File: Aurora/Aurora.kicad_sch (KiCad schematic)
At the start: 28 parts, among them J1 UJ20-C-H-C-3-SMT-TR, U1 STM32H757BITx

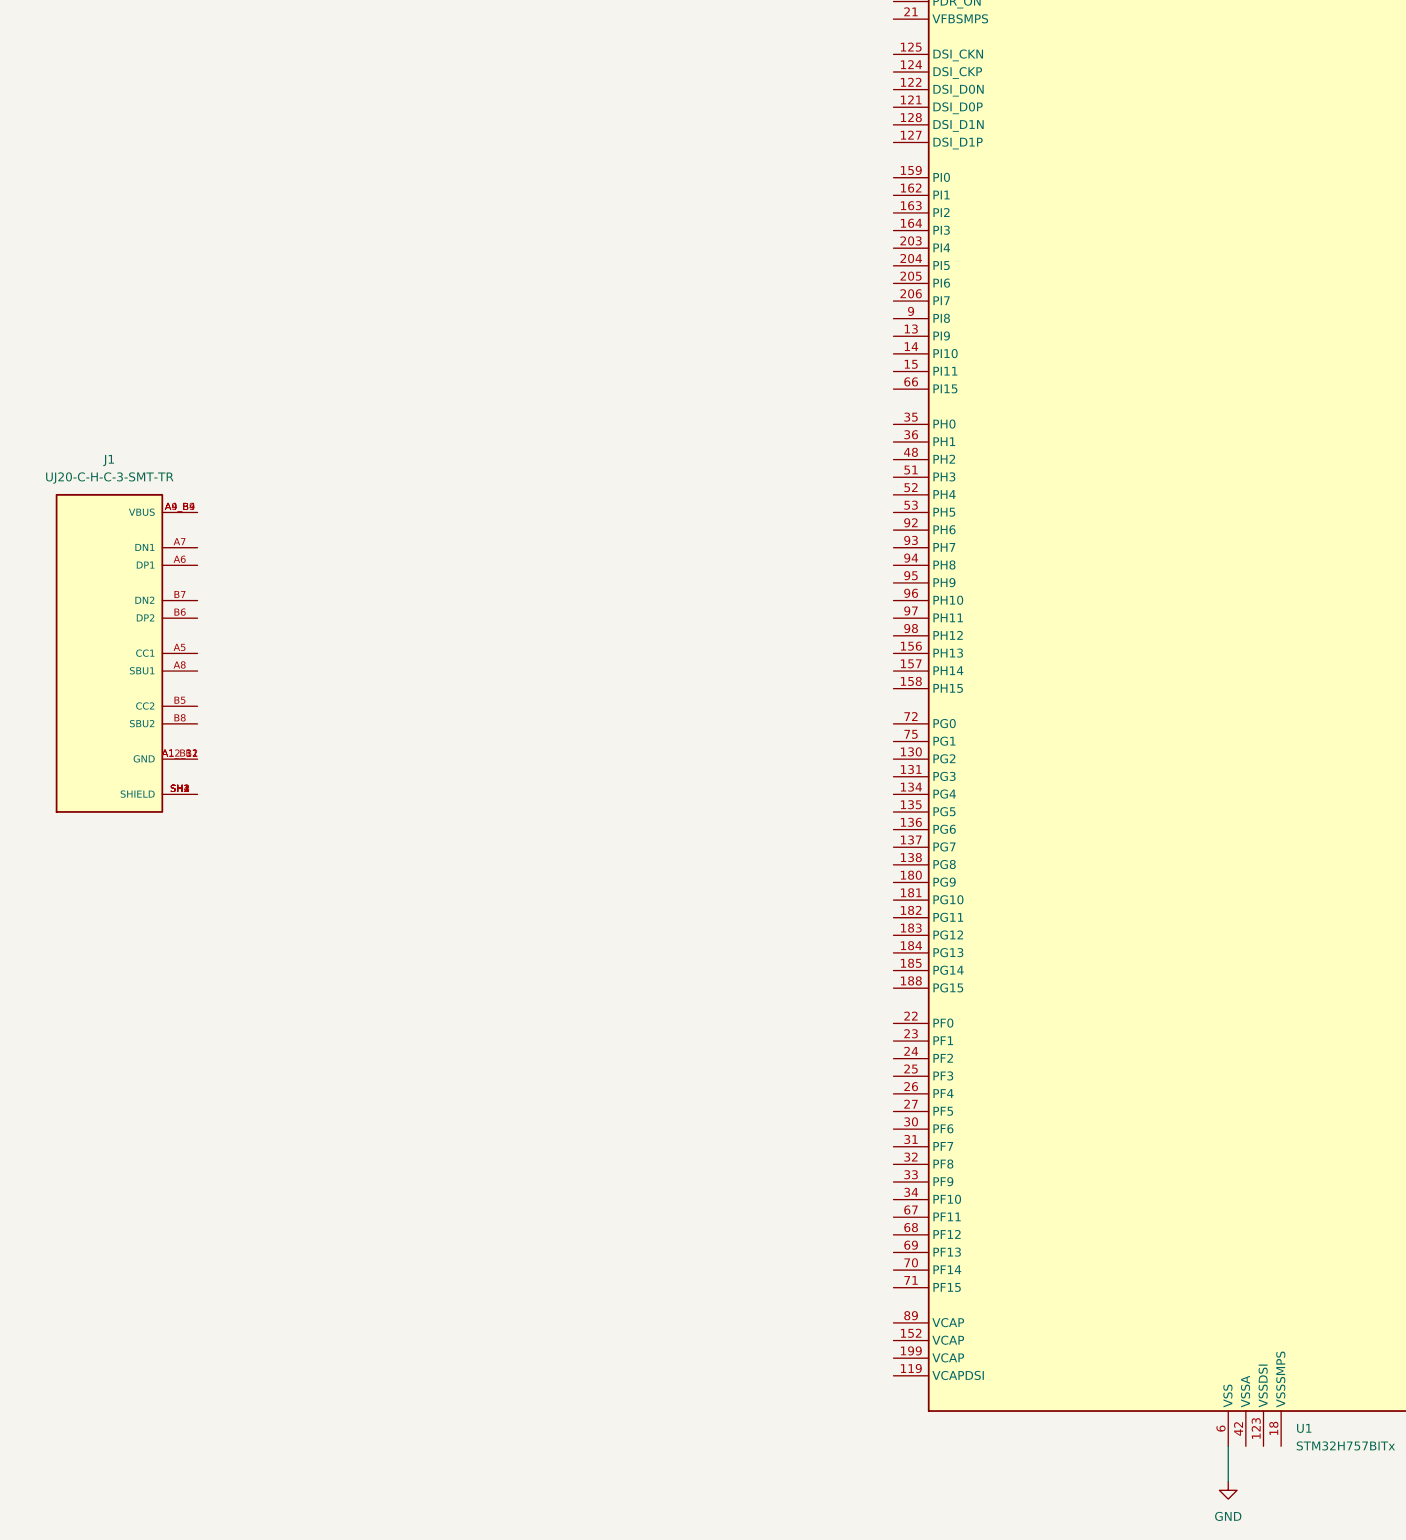
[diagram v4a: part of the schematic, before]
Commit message: hooked up USB receptacle, added ESD protection
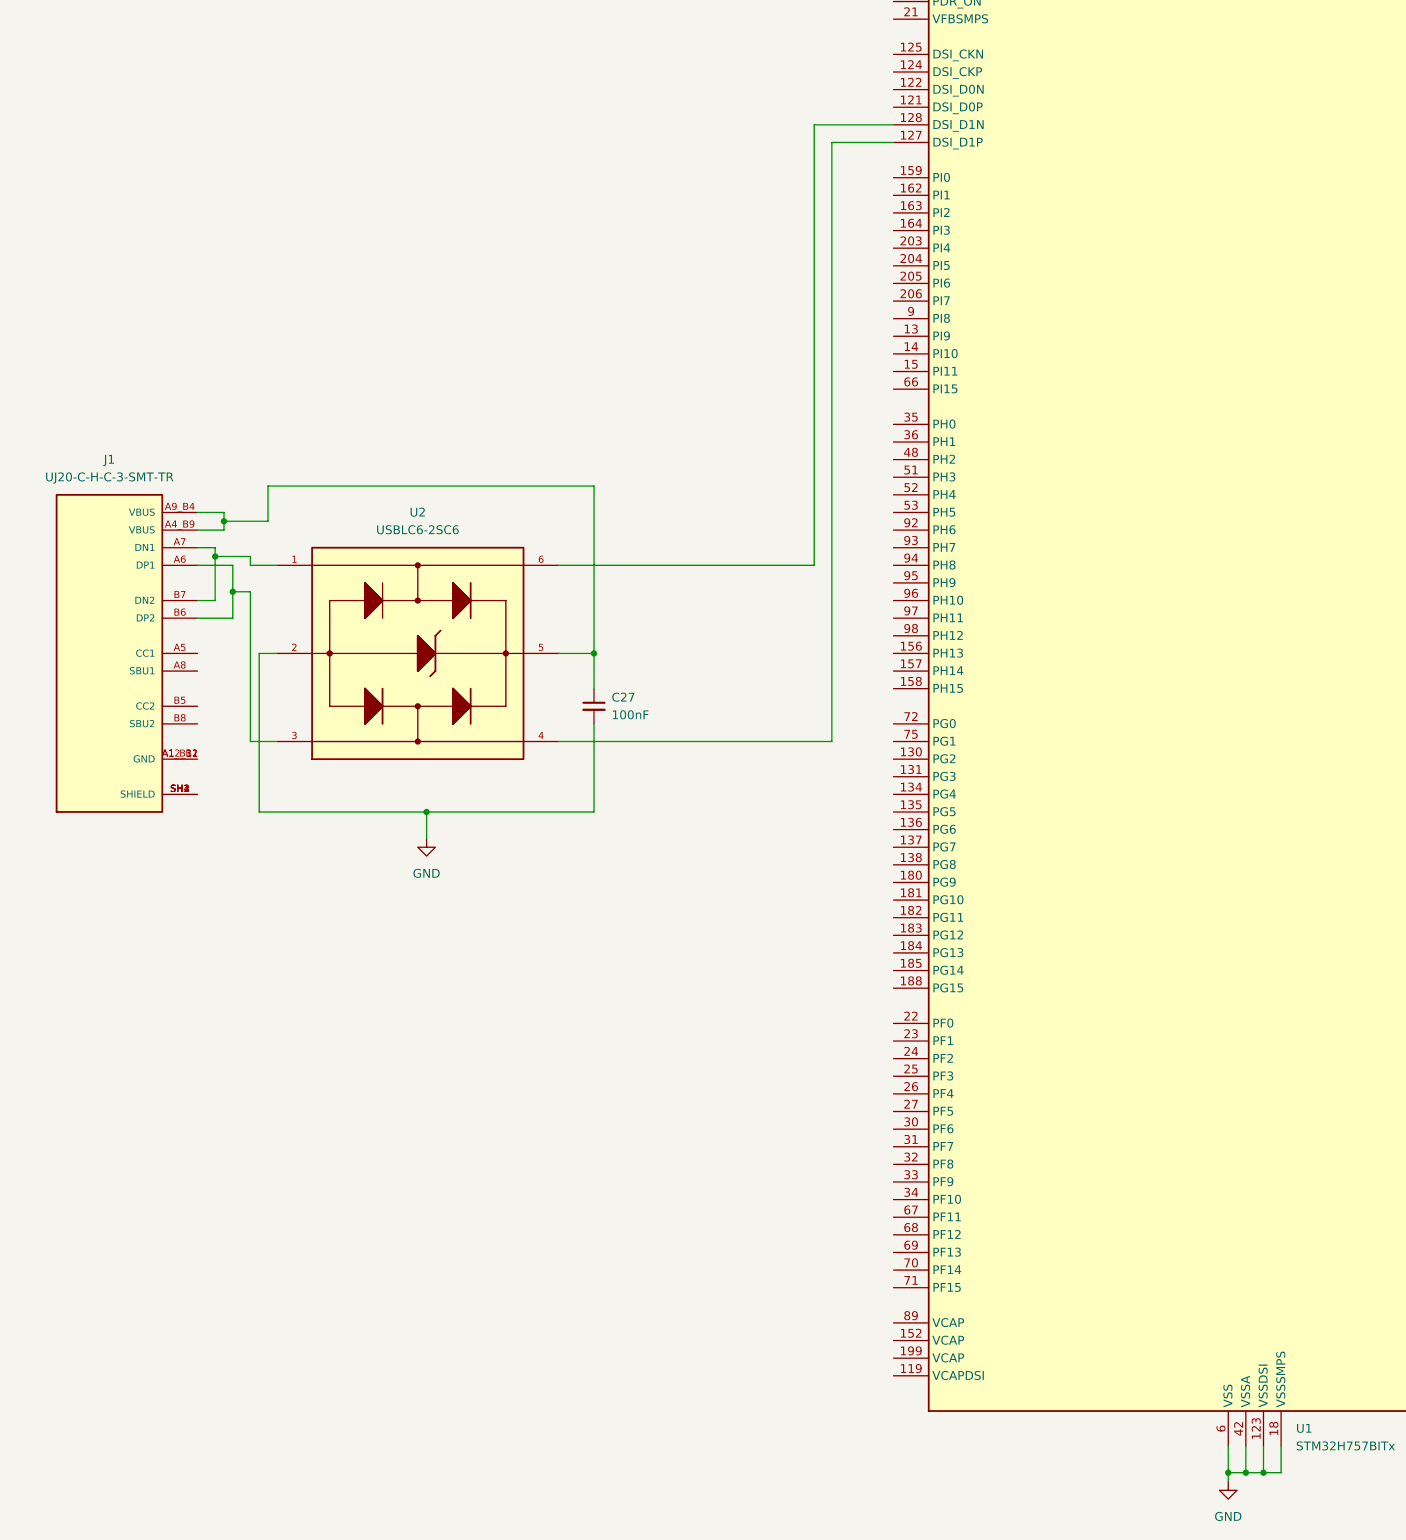
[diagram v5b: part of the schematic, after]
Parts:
- added C27: 100nF, symbol Device:C_Small
- added U2: USBLC6-2SC6, USBLC6-2SC6:SOT95P280X145-6N, symbol USBLC6-2SC6:USBLC6-2SC6
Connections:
- net GND: now also U1.123 (VSSDSI), U1.129 (VSSDSI), U1.18 (VSSSMPS), U1.42 (VSSA), C27.2, U2.2
- net at U1.127 (DSI_D1P): now also U2.4
- net at U1.128 (DSI_D1N): now also U2.6
- net at J1.A4_B9 (VBUS), J1.A9_B4 (VBUS): now also C27.1, U2.5
- net at J1.A6 (DP1): now also J1.B6 (DP2), U2.3
- net at J1.A7 (DN1): now also J1.B7 (DN2), U2.1

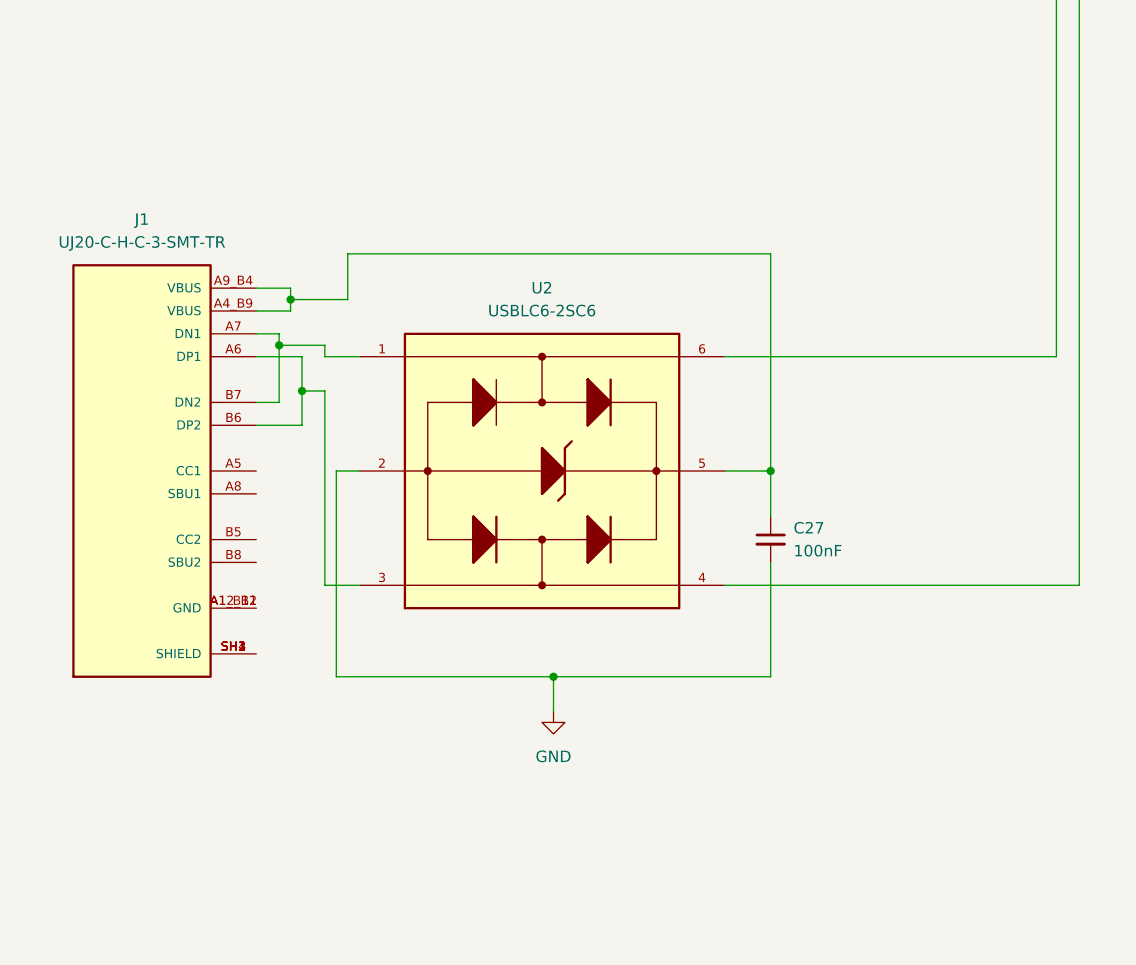
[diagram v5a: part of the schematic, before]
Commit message: updates to USB connection
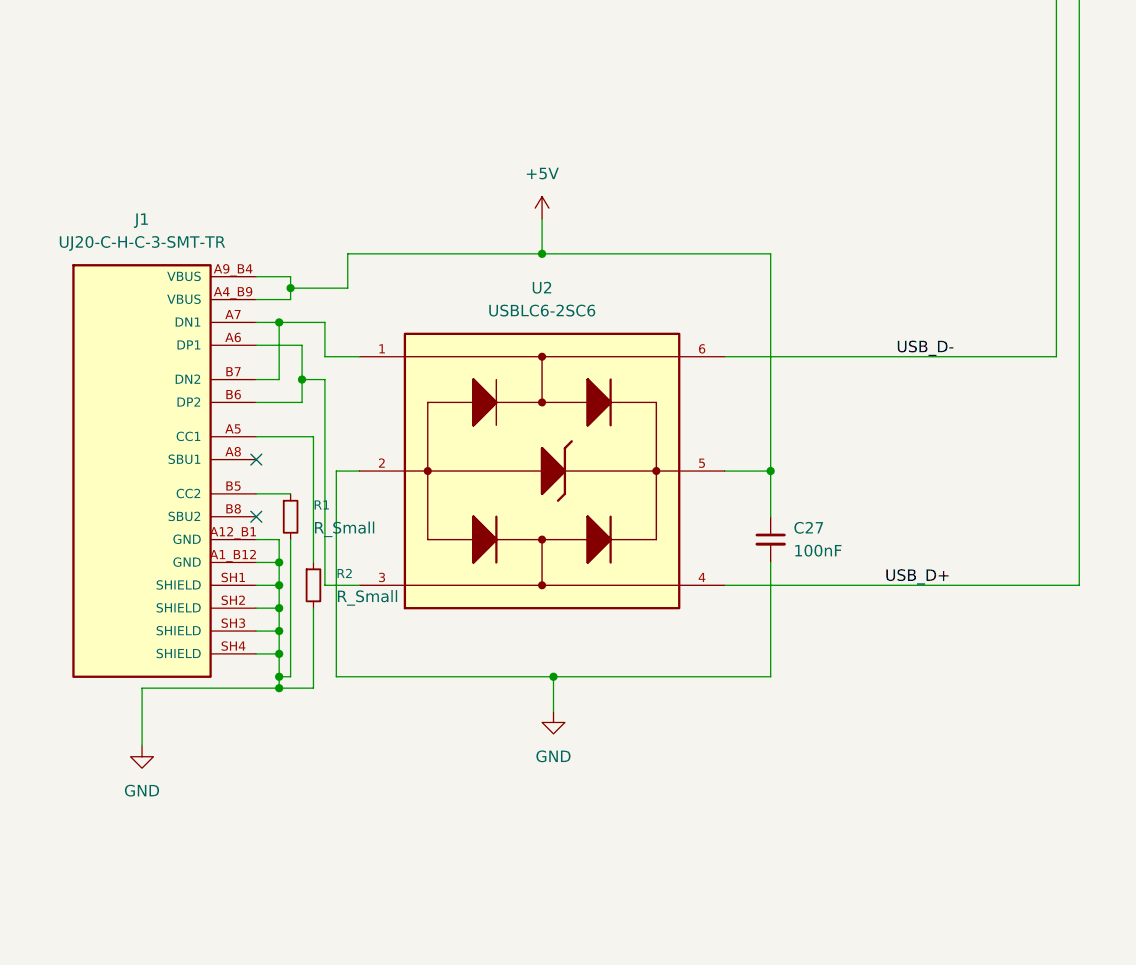
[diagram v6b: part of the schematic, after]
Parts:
- added R1, R2: R_Small, symbol Device:R_Small
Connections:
- net +5V: now also C27.1, J1.A4_B9 (VBUS), J1.A9_B4 (VBUS), U2.5
- net GND: now also J1.A12_B1 (GND), J1.A1_B12 (GND), J1.SH1 (SHIELD), J1.SH2 (SHIELD), J1.SH3 (SHIELD), J1.SH4 (SHIELD), R1.2, R2.2
- net USB_D+: now reaches U1.127 (DSI_D1P), U2.4
- net USB_D-: now reaches U1.128 (DSI_D1N), U2.6
- net at J1.A5 (CC1): now also R2.1
- net at J1.B5 (CC2): now also R1.1
- no-connect marks 0 -> 2
